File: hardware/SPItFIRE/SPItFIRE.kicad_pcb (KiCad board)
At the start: 2 copper layers, 114.3 x 83.8 mm, 44 parts, among them J1 Compact Host Joytsick/Mouse, J10 ISP, J11 Joystick A, J12 Joystick B, J13 Peripheral DE-9, J14 Peripheral User Port, J2 Host User Port, J3 User Port Passthrough, J4 SD Card Adapter, J5 DeadOnRTC, J6 SPI_4, J7 SPI_5, J8 SPI_6, J9 SPI_7, U1 74HC138, U2 ATmega1284P-A, Y1 Crystal

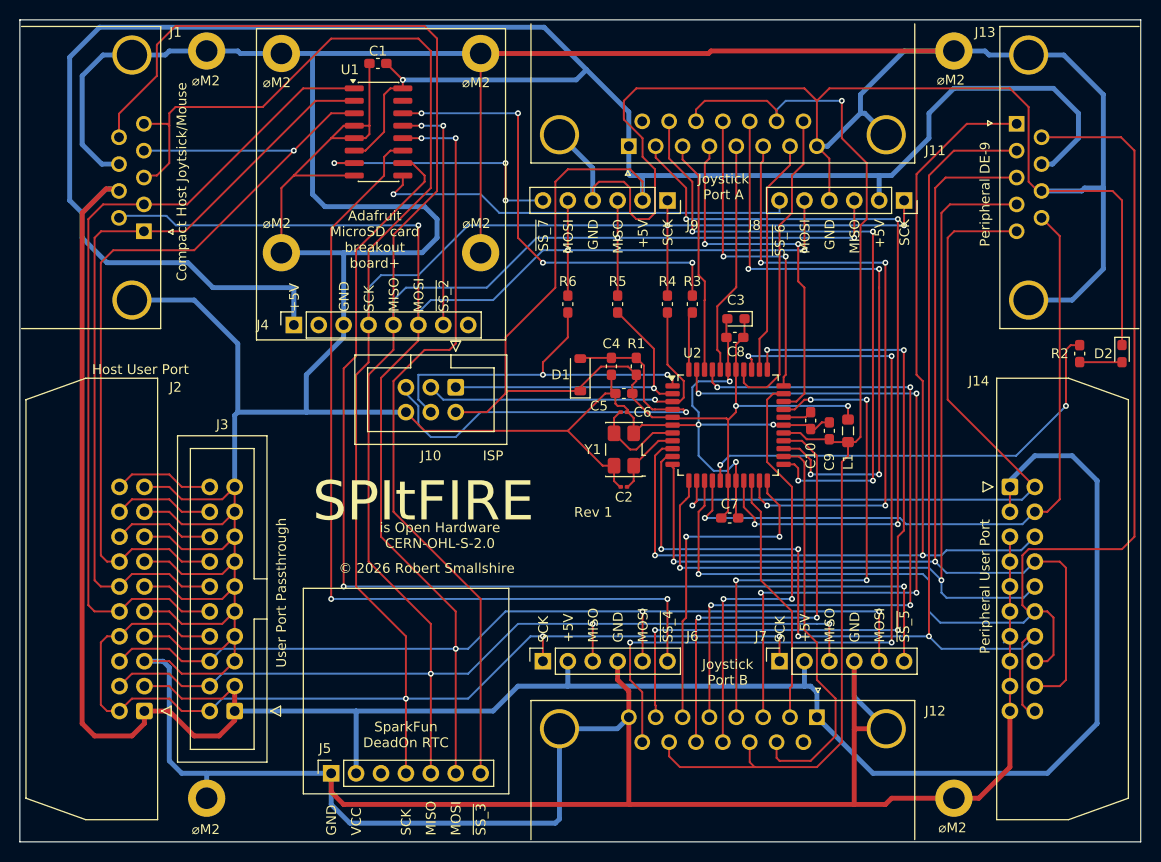
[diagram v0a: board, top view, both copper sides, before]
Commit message: Corrects the routing around the new corrected peripheral DE-9 connector
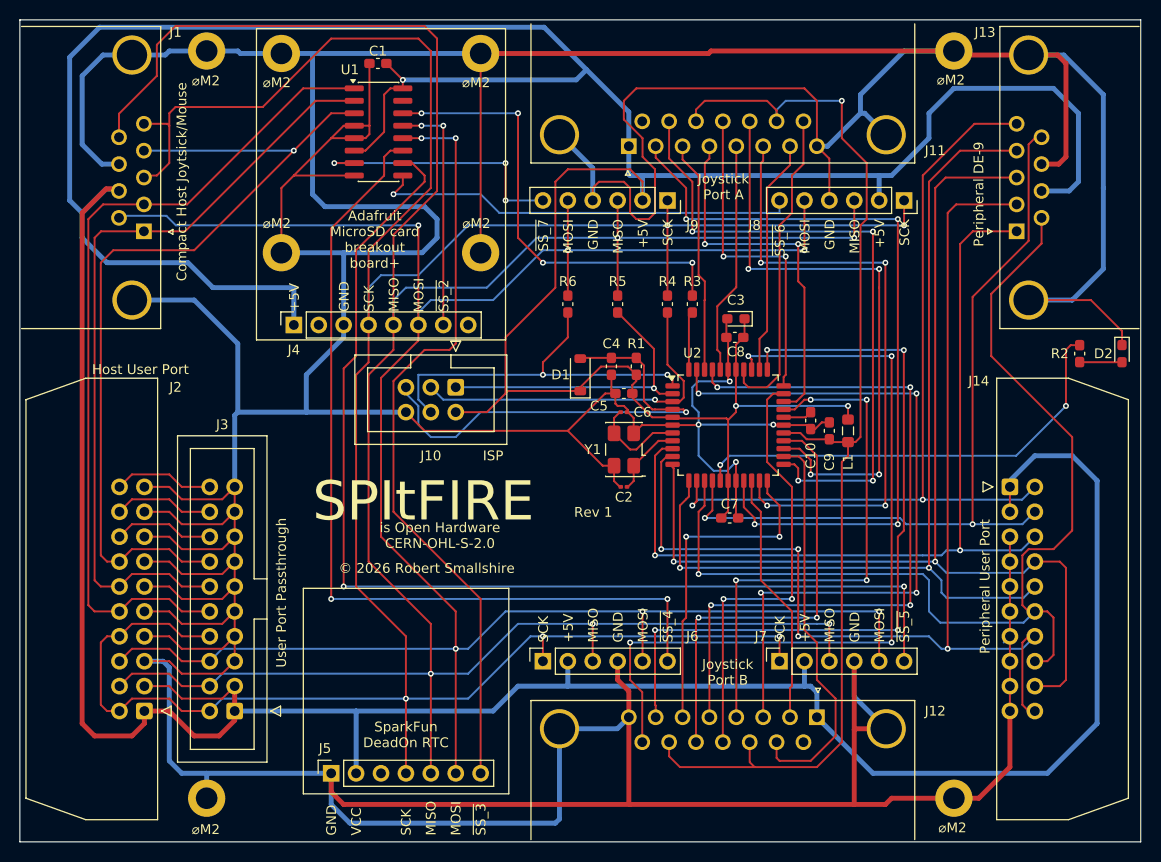
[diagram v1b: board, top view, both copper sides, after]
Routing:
- net GND: track 860.7 -> 827.5 mm
- net PD5: track 124.8 -> 106.8 mm
- net PD0: track 103.3 -> 89.3 mm
- net PD6: track 71.1 -> 81.3 mm, vias 1 -> 2
- net PD4: track 74.8 -> 83.3 mm, vias 1 -> 2
- net PD1: track 124.7 -> 119.6 mm
- net PD3: track 93.4 -> 97.6 mm
- net +5V: track 557.2 -> 561.3 mm

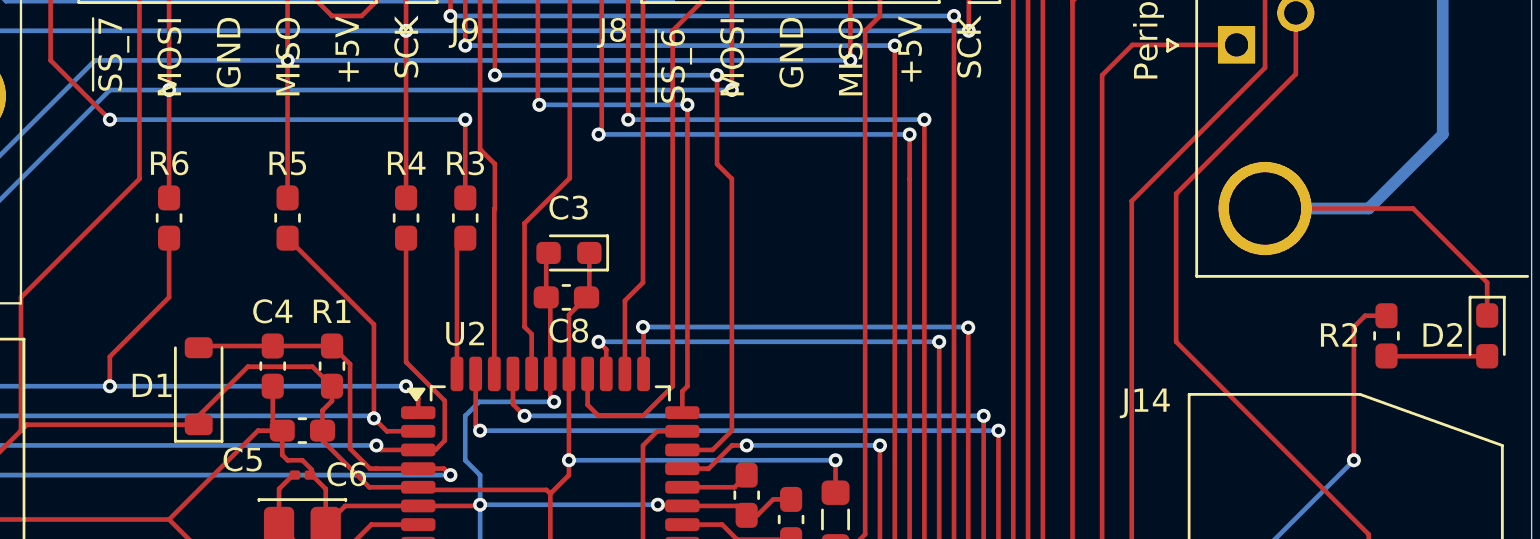
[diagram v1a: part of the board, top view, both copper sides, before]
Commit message: Use resistor footprints instead of capacitor footprints for the resistors
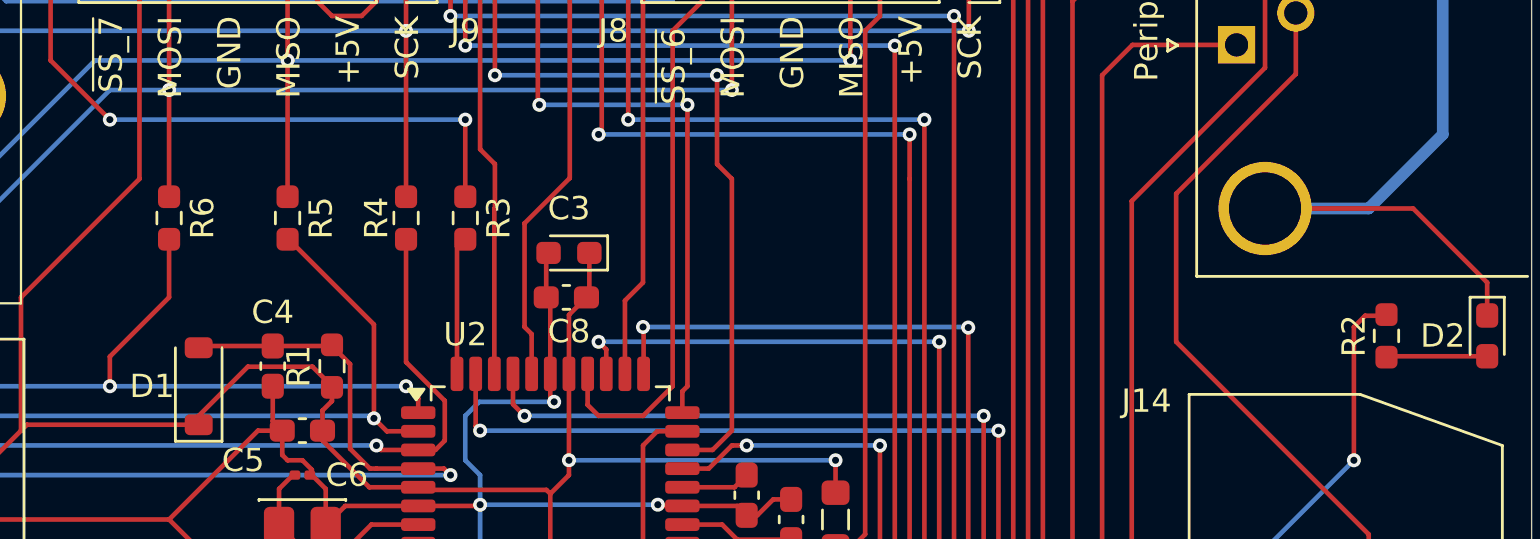
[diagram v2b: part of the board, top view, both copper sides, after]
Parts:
- R1, R2, R3, R4, R5, R6: footprint Capacitor_SMD:C_0603_1608Metric_Pad1.08x0.95mm_HandSolder -> Resistor_SMD:R_0603_1608Metric_Pad0.98x0.95mm_HandSolder

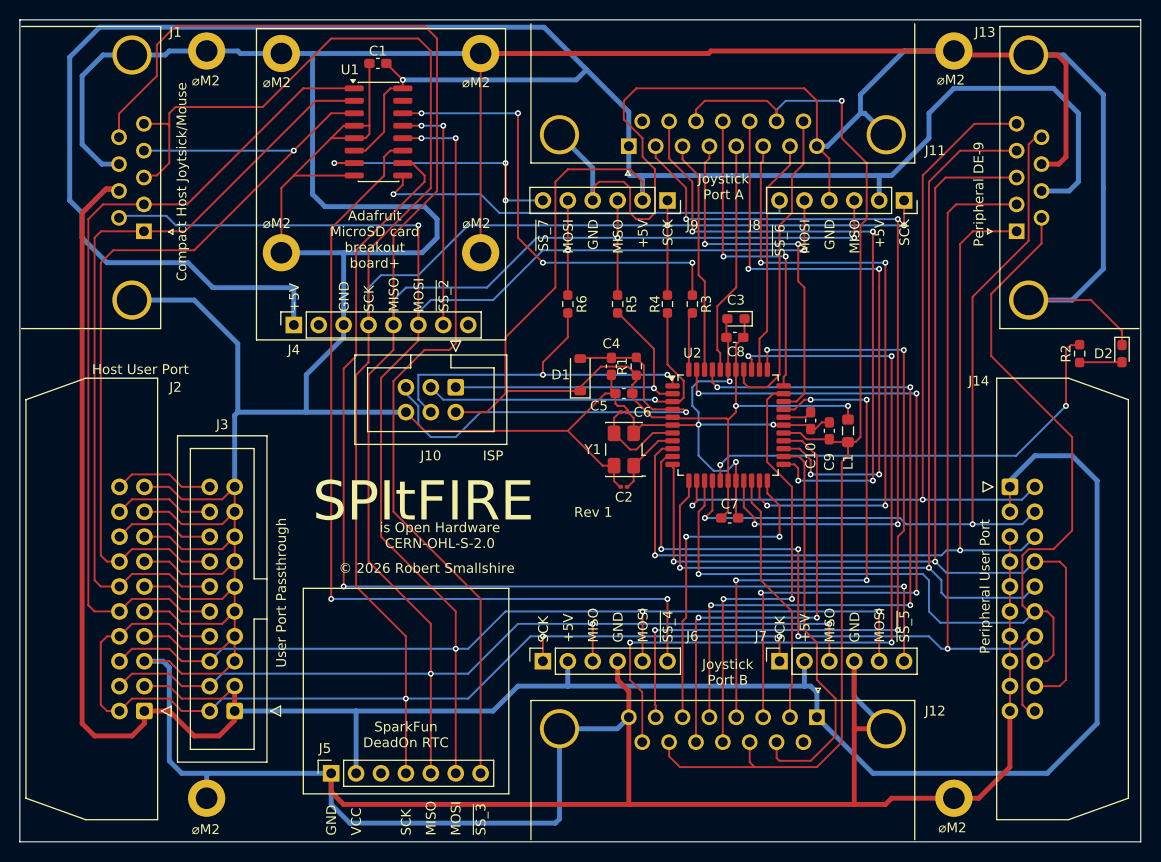
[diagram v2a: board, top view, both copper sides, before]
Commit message: Use updated footprints from the SPItFIRE library
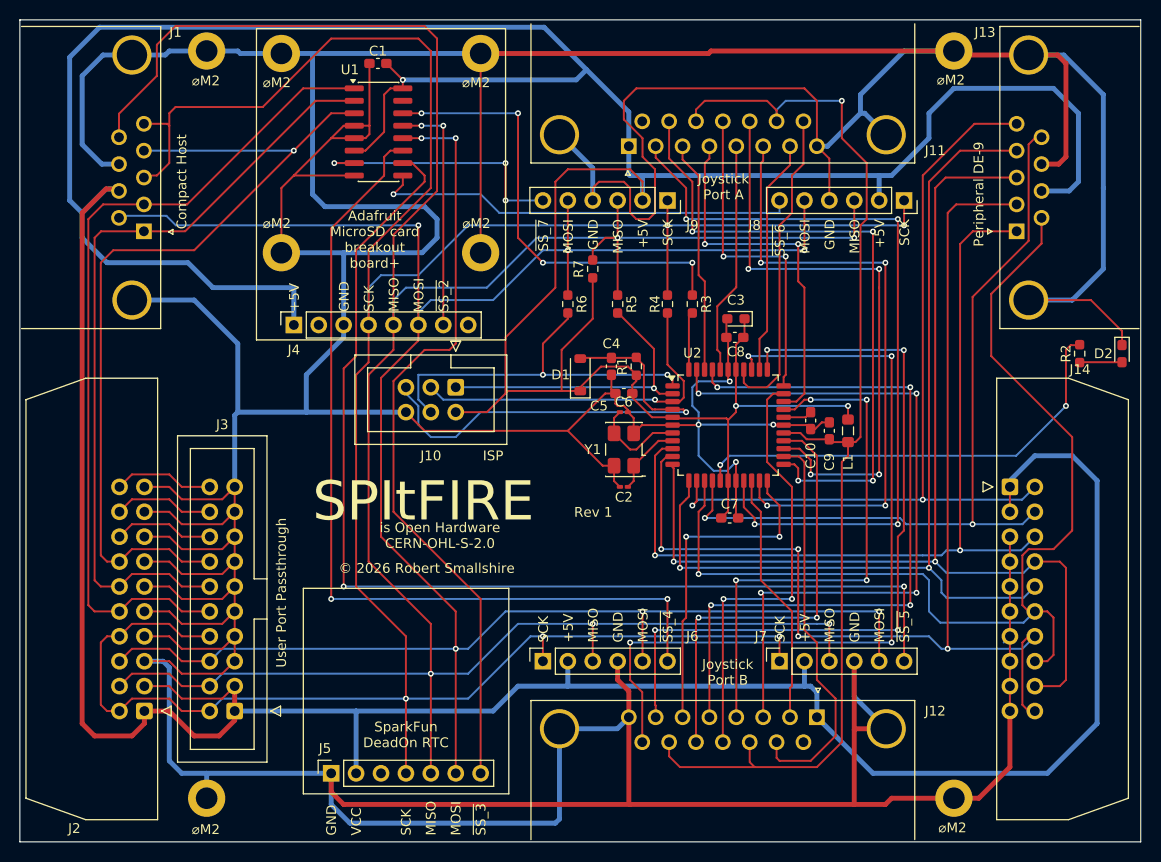
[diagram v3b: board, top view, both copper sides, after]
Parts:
- added R7: 10K, Resistor_SMD:R_0603_1608Metric_Pad0.98x0.95mm_HandSolder, F.Cu at (118.1, 75.6)
- C2, C6: value C_Small -> pF; footprint Capacitor_SMD:C_0201_0603Metric -> Capacitor_SMD:C_0201_0603Metric_Pad0.64x0.40mm_HandSolder
- J1: value Compact Host Joytsick/Mouse -> Compact Host
- J2: value Host User Port -> User Port Host
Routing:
- net +5V: track 561.3 -> 574.2 mm
- net MISO: track 265.5 -> 269.5 mm

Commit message: Reallocate the decoder outputs: Y7 is "no device"
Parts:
- C2, C6: value pF -> 27pF
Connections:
- J9 pad 6: ~{SS_7} -> ~{SS_0}
- U1 pad 15: unconnected-(U1-~{Y0}-Pad15) -> ~{SS_0}
- U1 pad 7: ~{SS_7} -> unconnected-(U1-~{Y7}-Pad7)
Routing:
- net ~{SS_7}: track 27.1 -> 0.00 mm, vias 3 -> 0
- net ~{SS_0}: track 0.00 -> 23.0 mm, vias 0 -> 1
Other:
- board text added: "~{SS_0}"
- board text removed: "~{SS_7}"
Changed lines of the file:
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@@
 			)
 		)
-		(property "Value" "pF"
+		(property "Value" "27pF"
 			(at 0 1.05 0)
 			(layer "F.Fab")
@@
 			)
 		)
-		(property "Value" "pF"
+		(property "Value" "27pF"
 			(at 0 1.05 180)
 			(layer "F.Fab")
@@
 			(layers "F.Cu" "F.Mask" "F.Paste")
 			(roundrect_rratio 0.25)
-			(net "~{SS_7}")
+			(net "unconnected-(U1-~{Y7}-Pad7)")
 			(pinfunction "~{Y7}_7")
-			(pintype "output")
+			(pintype "output+no_connect")
 		)
 		(pad "8" smd roundrect
@@
 			(layers "F.Cu" "F.Mask" "F.Paste")
 			(roundrect_rratio 0.25)
-			(net "unconnected-(U1-~{Y0}-Pad15)")
+			(net "~{SS_0}")
 			(pinfunction "~{Y0}_15")
-			(pintype "output+no_connect")
+			(pintype "output")
 		)
 		(pad "16" smd roundrect
@@
 			(layers "*.Cu" "*.Mask")
 			(remove_unused_layers no)
-			(net "~{SS_7}")
+			(net "~{SS_0}")
 			(pinfunction "Pin_6_6")
 			(pintype "passive")
@@
 		)
 	)
-	(gr_text "~{SS_7}"
+	(gr_text "~{SS_0}"
 		(at 113.665 70.485 90)
 		(layer "F.SilkS")
@@
 	)
 	(segment
-		(start 93.7925 64.77)
-		(end 91.7575 64.77)
-		(width 0.2)
-		(layer "F.Cu")
-		(net "~{SS_7}")
-	)
-	(segment
-		(start 109.22 68.58)
-		(end 109.22 64.77)
-		(width 0.2)
-		(layer "F.Cu")
-		(net "~{SS_7}")
-	)
-	(via
-		(at 91.7575 64.77)
-		(size 0.6)
-		(drill 0.3)
-		(layers "F.Cu" "B.Cu")
-		(net "~{SS_7}")
-	)
-	(via
-		(at 109.22 68.58)
-		(size 0.6)
-		(drill 0.3)
-		(layers "F.Cu" "B.Cu")
-		(net "~{SS_7}")
-	)
-	(via
-		(at 109.22 64.77)
-		(size 0.6)
-		(drill 0.3)
-		(layers "F.Cu" "B.Cu")
-		(net "~{SS_7}")
-	)
-	(segment
-		(start 109.22 64.77)
-		(end 91.7575 64.77)
-		(width 0.2)
-		(layer "B.Cu")
-		(net "~{SS_7}")
-	)
-	(segment
-		(start 109.22 68.58)
-		(end 113.03 68.58)
-		(width 0.2)
-		(layer "B.Cu")
-		(net "~{SS_7}")
-	)
-	(segment
 		(start 98.7425 66.9925)
 		(end 97.79 67.945)
@@
 		(net "Net-(J2-Pin_20)")
 	)
+	(segment
+		(start 98.7425 58.42)
+		(end 100.584 58.42)
+		(width 0.2)
+		(layer "F.Cu")
+		(net "~{SS_0}")
+	)
+	(via
+		(at 100.584 58.42)
+		(size 0.6)
+		(drill 0.3)
+		(layers "F.Cu" "B.Cu")
+		(net "~{SS_0}")
+	)
+	(segment
+		(start 113.03 68.58)
+		(end 113.03 67.056)
+		(width 0.2)
+		(layer "B.Cu")
+		(net "~{SS_0}")
+	)
+	(segment
+		(start 111.506 59.436)
+		(end 110.49 58.42)
+		(width 0.2)
+		(layer "B.Cu")
+		(net "~{SS_0}")
+	)
+	(segment
+		(start 110.49 58.42)
+		(end 100.584 58.42)
+		(width 0.2)
+		(layer "B.Cu")
+		(net "~{SS_0}")
+	)
+	(segment
+		(start 111.506 65.532)
+		(end 111.506 59.436)
+		(width 0.2)
+		(layer "B.Cu")
+		(net "~{SS_0}")
+	)
+	(segment
+		(start 113.03 67.056)
+		(end 111.506 65.532)
+		(width 0.2)
+		(layer "B.Cu")
+		(net "~{SS_0}")
+	)
 	(group ""
